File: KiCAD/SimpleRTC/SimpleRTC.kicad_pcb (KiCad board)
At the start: 2 copper layers, 44.5 x 21.6 mm, 19 parts, among them J1 AVR-ISP-6, J2 Conn_01x04, J3 Conn_01x04, U1 ATtiny85-20P

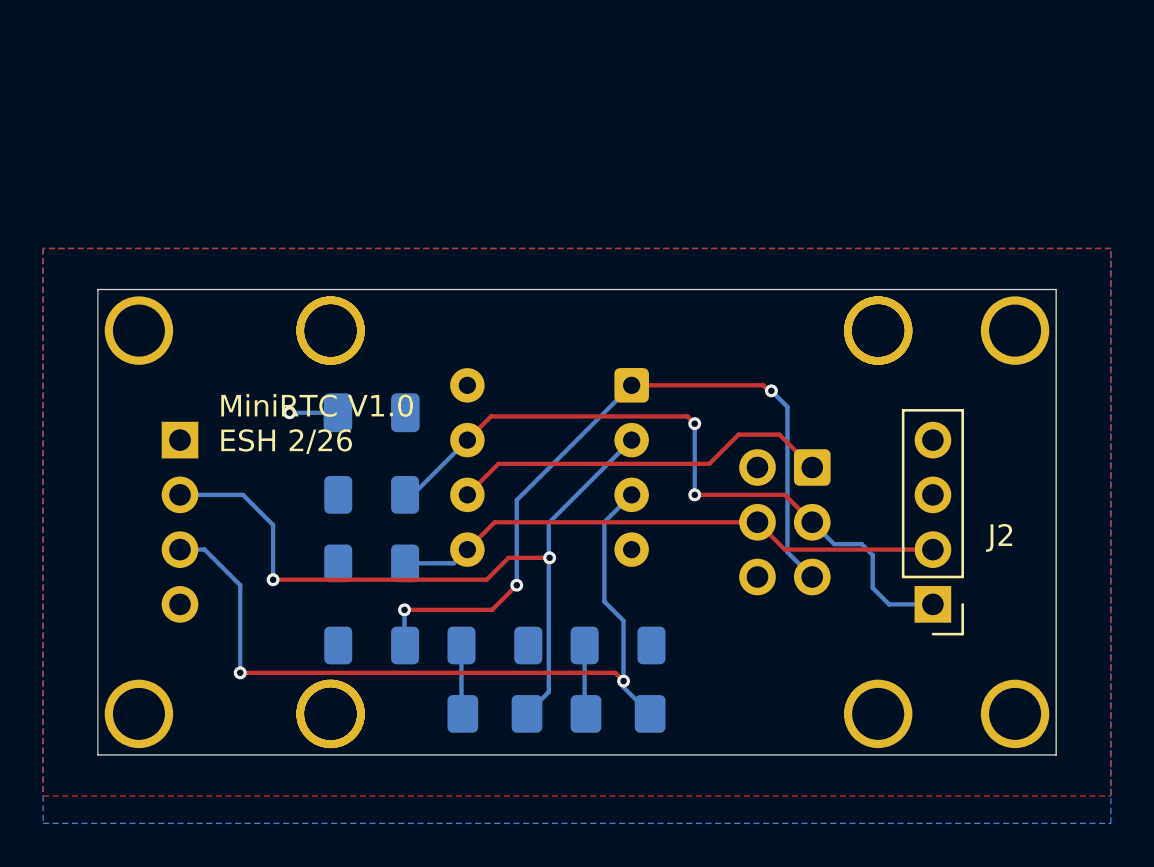
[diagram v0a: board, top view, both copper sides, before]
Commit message: add buttons to simple RTC, change to ATTiny84
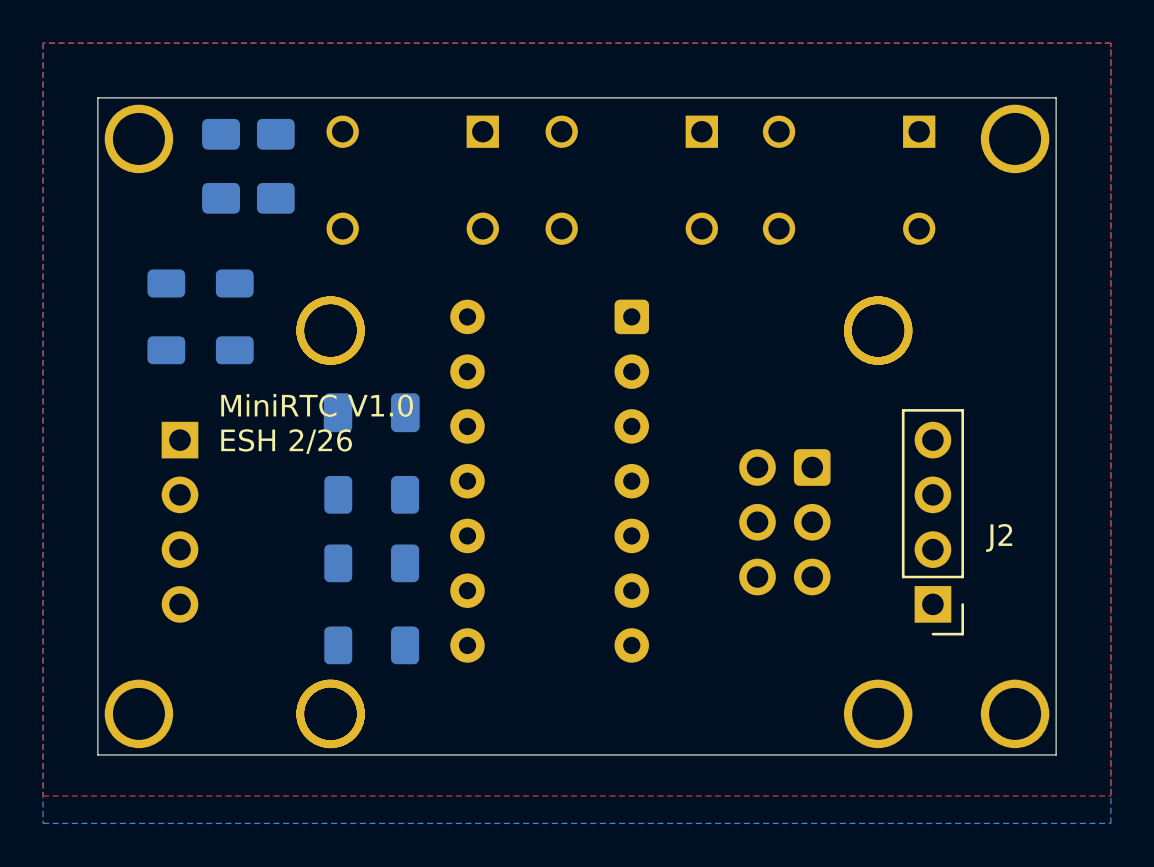
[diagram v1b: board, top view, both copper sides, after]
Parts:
- removed U1: ATtiny85-20P, Package_DIP:DIP-8_W7.62mm
- added SW1: SW_Push_pins13, AA_parts:SW4_1825910-B_TEC, B.Cu at (131.9, 41.0)
- added SW2: SW_Push_pins13, AA_parts:SW4_1825910-B_TEC, B.Cu at (121.8, 41.0)
- added SW3: SW_Push_pins13, AA_parts:SW4_1825910-B_TEC, B.Cu at (111.7, 41.0)
- added U2: ATtiny84A-P, Package_DIP:DIP-14_W7.62mm, B.Cu at (125.1, 45.1)
- moved D2 30.0 mm to (108.6, 38.1), turned to -90 degrees
- moved D1 28.4 mm to (106.0, 38.1), turned to -90 degrees
- moved R5 23.4 mm to (106.7, 45.1), turned to -90 degrees
- moved R3 21.6 mm to (103.5, 45.1), turned to -90 degrees
- moved H4 8.89 mm to (142.9, 36.8)
- moved H5 8.89 mm to (102.2, 36.8)
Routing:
- net /RX: track 37.0 -> 0.00 mm, vias 2 -> 0
- net /TX: track 35.4 -> 0.00 mm, vias 2 -> 0
- net /~{RST}: track 34.8 -> 0.00 mm, vias 3 -> 0
- net /SCK: track 32.4 -> 0.00 mm, vias 2 -> 0
- net /MOSI: track 25.8 -> 0.00 mm
- net /MISO: track 17.8 -> 0.00 mm
- net Net-(D2-A): track 3.20 -> 0.00 mm
- net Net-(D1-A): track 3.20 -> 0.00 mm
- net GND: track 2.25 -> 0.00 mm, vias 1 -> 0
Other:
- board size 44.5 x 21.6 mm -> 44.5 x 30.5 mm

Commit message: As built SimpleRTC design
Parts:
- removed H1, H2, H3: MountingHole, my_RTC:mtg_hole_256
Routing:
- net /RX: track 0.00 -> 49.2 mm, vias 0 -> 2
- net /SCK: track 0.00 -> 41.1 mm, vias 0 -> 3
- net /MOSI: track 0.00 -> 37.3 mm, vias 0 -> 2
- net /SW1: track 0.00 -> 29.3 mm, vias 0 -> 1
- net /~{RST}: track 0.00 -> 27.5 mm, vias 0 -> 2
- net /SW2: track 0.00 -> 25.7 mm, vias 0 -> 1
- net /TX: track 0.00 -> 24.9 mm, vias 0 -> 2
- net /MISO: track 0.00 -> 24.4 mm, vias 0 -> 1
- net /SW3: track 0.00 -> 19.5 mm
- net Net-(D1-A): track 0.00 -> 5.00 mm
- net Net-(D2-A): track 0.00 -> 4.74 mm
- net GND: track 0.00 -> 1.91 mm, vias 0 -> 1
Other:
- board text added: "MiniRTC V1.0 ESH 3/26"
- board text removed: "MiniRTC V1.0 ESH 2/26"

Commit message: modifying layout for V2
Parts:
- added H1: MountingHole, my_RTC:mtg_hole_256, F.Cu at (1.59, 1.59)
- added H2: MountingHole, my_RTC:mtg_hole_256, F.Cu at (1.59, 5.76)
- added H3: MountingHole, my_RTC:mtg_hole_256, F.Cu at (1.59, 9.94)
- SW1, SW2, SW3: footprint AA_parts:SW4_1825910-B_TEC -> AA_parts:SW_1437565-3
- moved H6 54.6 mm to (155.6, 51.7)
- moved H5 54.4 mm to (155.6, 47.5)
- moved R5 21.0 mm to (85.7, 43.8)
- moved D1 21.0 mm to (85.1, 36.8)
- moved D2 21.0 mm to (87.6, 36.8)
- moved R3 21.0 mm to (82.5, 43.8)
- moved H7 14.8 mm to (155.6, 55.9)
- moved H4 14.3 mm to (155.6, 43.4)
- moved SW1 9.03 mm to (139.2, 35.6)
- moved SW3 7.73 mm to (106.1, 35.6)
- moved SW2 5.46 mm to (122.7, 35.6)
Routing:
- net /RX: track 49.2 -> 0.00 mm, vias 2 -> 0
- net /SCK: track 41.1 -> 0.00 mm, vias 3 -> 0
- net /MOSI: track 37.3 -> 0.00 mm, vias 2 -> 0
- net /SW1: track 29.3 -> 0.00 mm, vias 1 -> 0
- net /~{RST}: track 27.5 -> 0.00 mm, vias 2 -> 0
- net /SW2: track 25.7 -> 0.00 mm, vias 1 -> 0
- net /TX: track 24.9 -> 0.00 mm, vias 2 -> 0
- net /MISO: track 24.4 -> 0.00 mm, vias 1 -> 0
- net /SW3: track 19.5 -> 0.00 mm
- net Net-(D1-A): track 5.00 -> 0.00 mm
- net Net-(D2-A): track 4.74 -> 0.00 mm
- net GND: track 1.91 -> 0.00 mm, vias 1 -> 0
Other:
- board size 44.5 x 30.5 mm -> 51.4 x 36.8 mm
